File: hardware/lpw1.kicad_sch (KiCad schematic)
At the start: 12 parts, among them J7 JST PH2P ST, Q2 DMG2305UXQ-7, U9 MCP73831-2

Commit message: Changed pins for J3 connector as it's sufficient to have I2C1 (GP18, GP19) for SDA/SCL, does not need ADC; V_BATT_MEASURE now uses GP28 with the built-in ADC; Connector J12 now uses 3.3V as well (from VCC); Improved layout;
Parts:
- R13, R14: footprint R_0603_1608Metric -> Resistor_SMD:R_0603_1608Metric
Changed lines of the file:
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@@
 		)
 	)
-	(global_label "V_BATT_MEASURE"
+	(global_label "V_IN"
 		(shape output)
-		(at 205.74 134.62 0)
+		(at 147.32 43.18 180)
 		(fields_autoplaced yes)
 		(effects
@@
 				(size 0.9906 0.9906)
 			)
-			(justify left)
+			(justify right)
 		)
 		(property "Intersheetrefs" "${INTERSHEET_REFS}"
-			(at 220.0112 134.62 0)
-			(effects
-				(font
-					(size 1.27 1.27)
-				)
-				(justify left)
-				(hide yes)
-			)
-		)
-	)
-	(global_label "CHARGE_STAT"
-		(shape bidirectional)
-		(at 111.76 142.24 0)
+			(at 142.3887 43.18 0)
+			(effects
+				(font
+					(size 1.27 1.27)
+				)
+				(justify right)
+				(hide yes)
+			)
+		)
+	)
+	(global_label "VSYS"
+		(shape input)
+		(at 109.22 66.04 0)
 		(fields_autoplaced yes)
 		(effects
@@
 		)
 		(property "Intersheetrefs" "${INTERSHEET_REFS}"
-			(at 124.1326 142.24 0)
+			(at 114.623 66.04 0)
 			(effects
 				(font
@@
 	)
 	(global_label "V_IN"
-		(shape output)
-		(at 147.32 43.18 180)
+		(shape input)
+		(at 96.52 66.04 180)
 		(fields_autoplaced yes)
 		(effects
@@
 		)
 		(property "Intersheetrefs" "${INTERSHEET_REFS}"
-			(at 142.3887 43.18 0)
+			(at 91.5887 66.04 0)
 			(effects
 				(font
@@
 		)
 	)
-	(global_label "VSYS"
+	(global_label "V_PWR_SWITCH"
 		(shape input)
-		(at 109.22 66.04 0)
+		(at 147.32 45.72 180)
 		(fields_autoplaced yes)
 		(effects
@@
 				(size 0.9906 0.9906)
 			)
-			(justify left)
+			(justify right)
 		)
 		(property "Intersheetrefs" "${INTERSHEET_REFS}"
-			(at 114.623 66.04 0)
-			(effects
-				(font
-					(size 1.27 1.27)
-				)
-				(justify left)
-				(hide yes)
-			)
-		)
-	)
-	(global_label "V_IN"
-		(shape input)
-		(at 96.52 66.04 180)
+			(at 134.6999 45.72 0)
+			(effects
+				(font
+					(size 1.27 1.27)
+				)
+				(justify right)
+				(hide yes)
+			)
+		)
+	)
+	(global_label "V_PWR_SWITCH"
+		(shape output)
+		(at 73.66 66.04 0)
 		(fields_autoplaced yes)
 		(effects
@@
 				(size 0.9906 0.9906)
 			)
-			(justify right)
+			(justify left)
 		)
 		(property "Intersheetrefs" "${INTERSHEET_REFS}"
-			(at 91.5887 66.04 0)
-			(effects
-				(font
-					(size 1.27 1.27)
-				)
-				(justify right)
-				(hide yes)
-			)
-		)
-	)
-	(global_label "V_PWR_SWITCH"
-		(shape input)
-		(at 147.32 45.72 180)
+			(at 86.2801 66.04 0)
+			(effects
+				(font
+					(size 1.27 1.27)
+				)
+				(justify left)
+				(hide yes)
+			)
+		)
+	)
+	(hierarchical_label "CHARGE_STAT"
+		(shape output)
+		(at 111.76 142.24 0)
 		(fields_autoplaced yes)
 		(effects
@@
 				(size 0.9906 0.9906)
 			)
-			(justify right)
-		)
-		(property "Intersheetrefs" "${INTERSHEET_REFS}"
-			(at 134.6999 45.72 0)
-			(effects
-				(font
-					(size 1.27 1.27)
-				)
-				(justify right)
-				(hide yes)
-			)
-		)
-	)
-	(global_label "V_PWR_SWITCH"
+			(justify left)
+		)
+	)
+	(hierarchical_label "V_BATT_VD_SWITCH"
 		(shape output)
-		(at 73.66 66.04 0)
+		(at 195.58 152.4 180)
 		(fields_autoplaced yes)
 		(effects
@@
 				(size 0.9906 0.9906)
 			)
-			(justify left)
-		)
-		(property "Intersheetrefs" "${INTERSHEET_REFS}"
-			(at 86.2801 66.04 0)
-			(effects
-				(font
-					(size 1.27 1.27)
-				)
-				(justify left)
-				(hide yes)
-			)
-		)
-	)
-	(global_label "V_BATT_VD_SWITCH"
-		(shape bidirectional)
-		(at 195.58 152.4 180)
+			(justify right)
+		)
+	)
+	(hierarchical_label "V_BATT_MEASURE"
+		(shape output)
+		(at 205.74 134.62 0)
 		(fields_autoplaced yes)
 		(effects
@@
 				(size 0.9906 0.9906)
 			)
-			(justify right)
-		)
-		(property "Intersheetrefs" "${INTERSHEET_REFS}"
-			(at 179.3867 152.4 0)
-			(effects
-				(font
-					(size 1.27 1.27)
-				)
-				(justify right)
-				(hide yes)
-			)
+			(justify left)
 		)
 	)
@@
 			)
 		)
-		(property "Footprint" "R_0603_1608Metric"
+		(property "Footprint" "Resistor_SMD:R_0603_1608Metric"
 			(at 193.802 142.24 90)
 			(effects
@@
 			)
 		)
-		(property "Footprint" "R_0603_1608Metric"
+		(property "Footprint" "Resistor_SMD:R_0603_1608Metric"
 			(at 193.802 128.27 90)
 			(effects

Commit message: Removed PWR_FLAGS except for VSYS; Removed NT2 (obsolete); Updated Schematics PDF; Reduced V_PWR_SWITCH routes to 1 from 2 to make space for VCC due to it being routed around the mounting holes of connectors J8/9; Improved silkscreen; TVS Diodes routes size increased; Updated BOM;
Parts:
- C13, C14: Mouser (none) -> 81-GRM188Z71A475KE5J
- Q2: Mouser (none) -> 621-DMG2305UXQ-7
- R12: Mouser Part Number (none) -> 708-RMCF0603FT3K30
- R13, R14: Mouser Part Number (none) -> ERJ-PA3J121V
- S1: Mouser 450404015514 -> 710-450404015514
- U9: Mouser Part Number (none) -> 579-MCP73831T-2ACIOT
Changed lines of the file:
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@@
-	)
-	(junction
-		(at 50.8 48.26)
-		(diameter 0)
-		(color 0 0 0 0)
 	)
 	(junction
@@
 	)
 	(junction
-		(at 71.12 66.04)
-		(diameter 0)
-		(color 0 0 0 0)
-	)
-	(junction
 		(at 134.62 121.92)
 		(diameter 0)
@@
 	)
 	(junction
-		(at 99.06 66.04)
-		(diameter 0)
-		(color 0 0 0 0)
-	)
-	(junction
 		(at 104.14 66.04)
 		(diameter 0)
@@
 	(wire
 		(pts
-			(xy 68.58 66.04) (xy 71.12 66.04)
+			(xy 68.58 66.04) (xy 73.66 66.04)
 		)
 		(stroke
@@
 	(wire
 		(pts
-			(xy 71.12 66.04) (xy 73.66 66.04)
-		)
-		(stroke
-			(width 0)
-			(type default)
-		)
-	)
-	(wire
-		(pts
-			(xy 50.8 48.26) (xy 50.8 58.42)
+			(xy 50.8 45.72) (xy 50.8 58.42)
 		)
 		(stroke
@@
 	(wire
 		(pts
-			(xy 96.52 66.04) (xy 99.06 66.04)
+			(xy 96.52 66.04) (xy 104.14 66.04)
 		)
 		(stroke
@@
 	(wire
 		(pts
-			(xy 50.8 45.72) (xy 50.8 48.26)
-		)
-		(stroke
-			(width 0.1524)
-			(type solid)
-		)
-	)
-	(wire
-		(pts
 			(xy 68.58 35.56) (xy 68.58 36.83)
 		)
@@
 		(pts
 			(xy 195.58 134.62) (xy 205.74 134.62)
-		)
-		(stroke
-			(width 0)
-			(type default)
-		)
-	)
-	(wire
-		(pts
-			(xy 99.06 66.04) (xy 104.14 66.04)
 		)
 		(stroke
@@
 			)
 		)
+		(property "Mouser Part Number" "708-RMCF0603FT3K30"
+			(at 86.36 153.67 0)
+			(effects
+				(font
+					(size 1.27 1.27)
+				)
+				(hide yes)
+			)
+		)
 		(pin "1"
 		)
@@
 	)
 	(symbol
-		(lib_id "power:PWR_FLAG")
-		(at 50.8 48.26 90)
-		(unit 1)
-		(exclude_from_sim no)
-		(in_bom yes)
-		(on_board yes)
-		(dnp no)
-		(fields_autoplaced yes)
-		(property "Reference" "#FLG03"
-			(at 48.895 48.26 0)
-			(effects
-				(font
-					(size 1.27 1.27)
-				)
-				(hide yes)
-			)
-		)
-		(property "Value" "PWR_FLAG"
-			(at 46.99 48.2599 90)
-			(effects
-				(font
-					(size 1.27 1.27)
-				)
-				(justify left)
-			)
-		)
-		(property "Footprint" ""
-			(at 50.8 48.26 0)
-			(effects
-				(font
-					(size 1.27 1.27)
-				)
-				(hide yes)
-			)
-		)
-		(property "Datasheet" "~"
-			(at 50.8 48.26 0)
-			(effects
-				(font
-					(size 1.27 1.27)
-				)
-				(hide yes)
-			)
-		)
-		(property "Description" "Special symbol for telling ERC where power comes from"
-			(at 50.8 48.26 0)
-			(effects
-				(font
-					(size 1.27 1.27)
-				)
-				(hide yes)
-			)
-		)
-		(pin "1"
-		)
-		(instances
-			(project "FABI_schematic"
-				(path "/8404dabe-a0ce-44ce-a3c9-f9e9e54d2b02/793a4126-d8fb-49c3-b4dd-9f7725c17758"
-					(reference "#FLG03")
-					(unit 1)
-				)
-			)
-		)
-	)
-	(symbol
-		(lib_id "power:PWR_FLAG")
-		(at 71.12 66.04 180)
-		(unit 1)
-		(exclude_from_sim no)
-		(in_bom yes)
-		(on_board yes)
-		(dnp no)
-		(property "Reference" "#FLG04"
-			(at 71.12 67.945 0)
-			(effects
-				(font
-					(size 1.27 1.27)
-				)
-				(hide yes)
-			)
-		)
-		(property "Value" "PWR_FLAG"
-			(at 68.58 78.74 0)
-			(effects
-				(font
-					(size 1.27 1.27)
-				)
-			)
-		)
-		(property "Footprint" ""
-			(at 71.12 66.04 0)
-			(effects
-				(font
-					(size 1.27 1.27)
-				)
-				(hide yes)
-			)
-		)
-		(property "Datasheet" "~"
-			(at 71.12 66.04 0)
-			(effects
-				(font
-					(size 1.27 1.27)
-				)
-				(hide yes)
-			)
-		)
-		(property "Description" "Special symbol for telling ERC where power comes from"
-			(at 71.12 66.04 0)
-			(effects
-				(font
-					(size 1.27 1.27)
-				)
-				(hide yes)
-			)
-		)
-		(pin "1"
-		)
-		(instances
-			(project "FABI_schematic"
-				(path "/8404dabe-a0ce-44ce-a3c9-f9e9e54d2b02/793a4126-d8fb-49c3-b4dd-9f7725c17758"
-					(reference "#FLG04")
-					(unit 1)
-				)
-			)
-		)
-	)
-	(symbol
 		(lib_id "Connector:TestPoint_Probe")
 		(at 68.58 48.26 0)
@@
 			)
 		)
+		(property "Mouser" "621-DMG2305UXQ-7"
+			(at 60.96 58.42 0)
+			(effects
+				(font
+					(size 1.27 1.27)
+				)
+				(hide yes)
+			)
+		)
 		(pin "1"
 		)
@@
 		)
 		(property "Reichelt" ""
+			(at 101.6 139.7 0)
+			(effects
+				(font
+					(size 1.27 1.27)
+				)
+				(hide yes)
+			)
+		)
+		(property "Mouser Part Number" "579-MCP73831T-2ACIOT"
 			(at 101.6 139.7 0)
 			(effects
@@
 			)
 		)
-		(property "Mouser" "450404015514"
+		(property "Mouser" "710-450404015514"
 			(at 149.86 43.18 0)
 			(effects
@@
 	)
 	(symbol
-		(lib_id "power:PWR_FLAG")
-		(at 99.06 66.04 0)
-		(unit 1)
-		(exclude_from_sim no)
-		(in_bom yes)
-		(on_board yes)
-		(dnp no)
-		(fields_autoplaced yes)
-		(property "Reference" "#FLG05"
-			(at 99.06 64.135 0)
-			(effects
-				(font
-					(size 1.27 1.27)
-				)
-				(hide yes)
-			)
-		)
-		(property "Value" "PWR_FLAG"
-			(at 99.06 60.96 0)
-			(effects
-				(font
-					(size 1.27 1.27)
-				)
-			)
-		)
-		(property "Footprint" ""
-			(at 99.06 66.04 0)
-			(effects
-				(font
-					(size 1.27 1.27)
-				)
-				(hide yes)
-			)
-		)
-		(property "Datasheet" "~"
-			(at 99.06 66.04 0)
-			(effects
-				(font
-					(size 1.27 1.27)
-				)
-				(hide yes)
-			)
-		)
-		(property "Description" "Special symbol for telling ERC where power comes from"
-			(at 99.06 66.04 0)
-			(effects
-				(font
-					(size 1.27 1.27)
-				)
-				(hide yes)
-			)
-		)
-		(pin "1"
-		)
-		(instances
-			(project "FABI_schematic"
-				(path "/8404dabe-a0ce-44ce-a3c9-f9e9e54d2b02/793a4126-d8fb-49c3-b4dd-9f7725c17758"
-					(reference "#FLG05")
-					(unit 1)
-				)
-			)
-		)
-	)
-	(symbol
 		(lib_id "Device:R")
 		(at 195.58 142.24 0)
@@
 			)
 		)
+		(property "Mouser Part Number" "ERJ-PA3J121V"
+			(at 195.58 142.24 0)
+			(effects
+				(font
+					(size 1.27 1.27)
+				)
+				(hide yes)
+			)
+		)
 		(pin "1"
 		)
@@
 			)
 		)
+		(property "Mouser" "81-GRM188Z71A475KE5J"
+			(at 68.58 146.05 0)
+			(effects
+				(font
+					(size 1.27 1.27)
+				)
+				(hide yes)
+			)
+		)
 		(pin "1"
 		)
@@
 			)
 		)
+		(property "Mouser" "81-GRM188Z71A475KE5J"
+			(at 134.62 133.35 0)
+			(effects
+				(font
+					(size 1.27 1.27)
+				)
+				(hide yes)
+			)
+		)
 		(pin "1"
 		)
@@
 				)
 				(hide yes)
+			)
+		)
+		(property "Mouser Part Number" "ERJ-PA3J121V"
+			(at 195.58 128.27 0)
+			(effects
+				(font
+					(size 1.27 1.27)
+				)
+				(hide yes)

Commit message: Moved FABI Logo; Changed some names; Changed VSYS label on LPW1; Updated SCH PDF;
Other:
- note added: "Battery Switch"
- note removed: "Voltage Regulator"
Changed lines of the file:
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@@
 		)
 	)
-	(text "Voltage Regulator"
+	(text "Battery Switch\n"
 		(exclude_from_sim no)
 		(at 30.48 25.4 0)
@@
 				)
 				(justify right)
-				(hide yes)
-			)
-		)
-	)
-	(global_label "VSYS"
-		(shape input)
-		(at 109.22 66.04 0)
-		(fields_autoplaced yes)
-		(effects
-			(font
-				(size 0.9906 0.9906)
-			)
-			(justify left)
-		)
-		(property "Intersheetrefs" "${INTERSHEET_REFS}"
-			(at 114.623 66.04 0)
-			(effects
-				(font
-					(size 1.27 1.27)
-				)
-				(justify left)
 				(hide yes)
 			)
@@
 					(unit 1)
 				)
+			)
+		)
+	)
+	(symbol
+		(lib_id "power:VBUS")
+		(at 109.22 66.04 0)
+		(unit 1)
+		(exclude_from_sim no)
+		(in_bom yes)
+		(on_board yes)
+		(dnp no)
+		(property "Reference" "#PWR042"
+			(at 109.22 69.85 0)
+			(effects
+				(font
+					(size 1.27 1.27)
+				)
+				(hide yes)
+			)
+		)
+		(property "Value" "VSYS"
+			(at 109.22 62.23 0)
+			(effects
+				(font
+					(size 1.27 1.27)
+				)
+			)
+		)
+		(property "Footprint" ""
+			(at 109.22 66.04 0)
+			(effects
+				(font
+					(size 1.27 1.27)
+				)
+				(hide yes)
+			)
+		)
+		(property "Datasheet" ""
+			(at 109.22 66.04 0)
+			(effects
+				(font
+					(size 1.27 1.27)
+				)
+				(hide yes)
+			)
+		)
+		(property "Description" ""
+			(at 109.22 66.04 0)
+			(effects
+				(font
+					(size 1.27 1.27)
+				)
+				(hide yes)
+			)
+		)
+		(pin "1"
+		)
+		(instances
+			(project "FABI_schematic"
+				(path "/8404dabe-a0ce-44ce-a3c9-f9e9e54d2b02/793a4126-d8fb-49c3-b4dd-9f7725c17758"
+					(reference "#PWR042")
+					(unit 1)
+				)

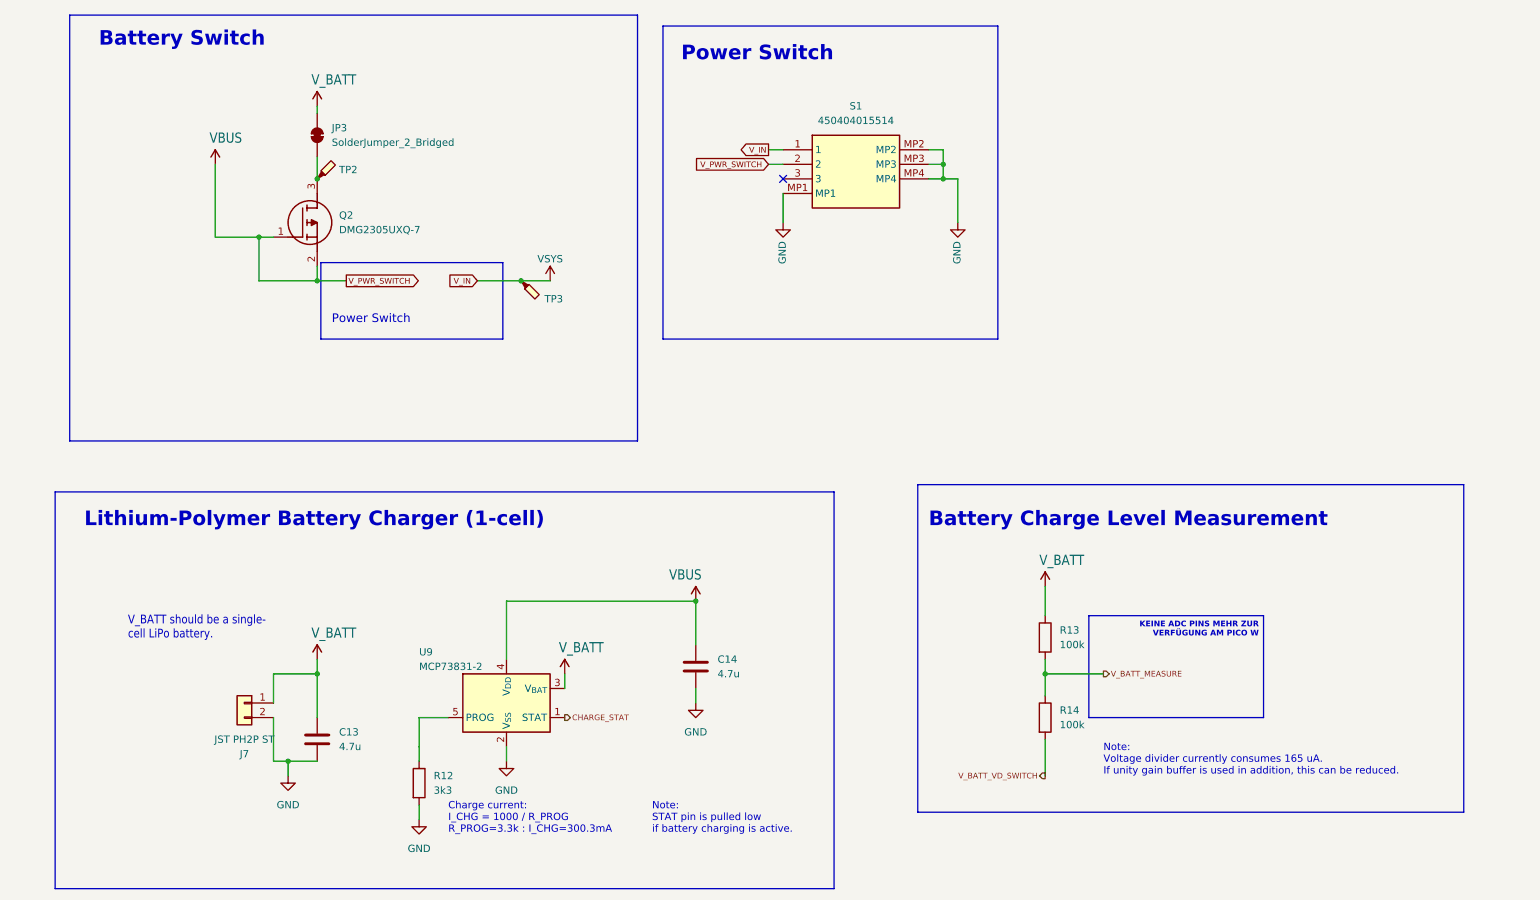
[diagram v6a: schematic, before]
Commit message: Added sheet comments
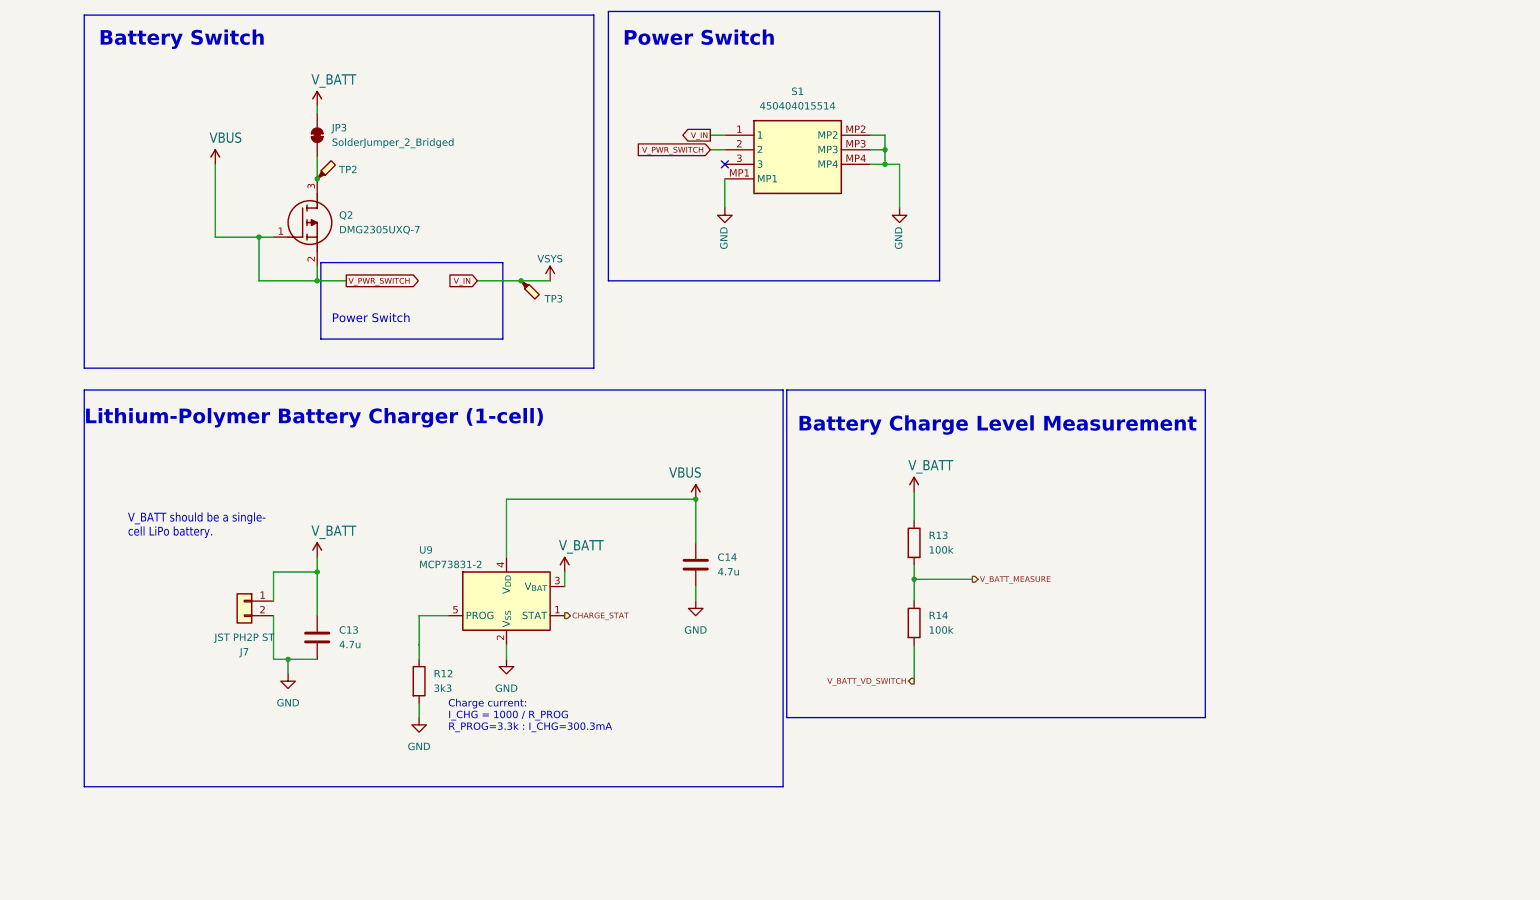
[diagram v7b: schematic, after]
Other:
- note removed: "Note: STAT pin is pulled low if battery charging is active."
- note removed: "Note: Voltage divider currently consumes 165 uA. If unity gain buffer is used in addition, this can be reduced."
- company: (none) -> Christoph Veigl & Jimmi Bacher
- title: (none) -> LPW
- moved on the sheet: C13, C14, J7, R12, R13, R14, S1, U9
